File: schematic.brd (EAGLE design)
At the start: 60.9 x 63.2 mm, 40 parts, among them CN1 1X4-BIG, CN2 1X4-BIG, IC3 78TO220, IC4 78TO220

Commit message: Initial board layout
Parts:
- moved R19 36.3 mm to (4.83, 21.8), turned to 180 degrees
- moved R3 25.2 mm to (9.14, 18.8), flipped to the bottom, turned to 180 degrees
- moved R8 24.2 mm to (9.14, 16.8), flipped to the bottom, turned to 180 degrees
- moved R6 22.3 mm to (9.14, 20.8), flipped to the bottom, turned to 180 degrees
- moved R18 18.8 mm to (25.1, 36.3), turned to 90 degrees
- moved R13 17.3 mm to (4.83, 36.3), turned to 270 degrees
- moved R17 17.1 mm to (6.86, 36.3), turned to 90 degrees
- moved R14 15.2 mm to (23.1, 36.3), turned to 270 degrees
- moved R10 13.5 mm to (9.14, 23.6), flipped to the bottom, turned to 180 degrees
- moved R2 13.1 mm to (21.1, 25.7)
- moved R7 13.1 mm to (21.1, 27.7), turned to 180 degrees
- moved R4 12.4 mm to (9.14, 25.7), flipped to the bottom, turned to 180 degrees
- moved R15 12.3 mm to (21.1, 30.7)
- moved R16 12.3 mm to (9.14, 30.7), turned to 180 degrees
- moved R9 12.3 mm to (21.1, 23.6), turned to 0 degrees
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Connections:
- net CTRL_A_3V3: now also U$1.P$23; no longer U$1.P$26
- net CTRL_B_3V3: now also U$1.P$26; no longer U$1.P$23
- net CTRL_G: now also U$1.P$27; no longer U$1.P$28
- net CTRL_R: now also U$1.P$28; no longer U$1.P$27
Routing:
- net +12V: track 0.00 -> 77.9 mm, vias 0 -> 1
- net +5V: track 0.00 -> 46.5 mm
- net N$7: track 0.00 -> 30.4 mm
- net N$5: track 0.00 -> 30.1 mm
- net CTRL_A_3V3: track 0.00 -> 29.2 mm, vias 0 -> 1
- net CTRL_G: track 0.00 -> 25.2 mm
- net CTRL_B: track 0.00 -> 23.3 mm
- net POW_B: track 0.00 -> 18.3 mm
- net N$6: track 0.00 -> 18.2 mm
- net N$8: track 0.00 -> 16.6 mm
- net POW_R: track 0.00 -> 16.4 mm
- net GND: track 0.00 -> 16.3 mm, vias 0 -> 1
- net +3V3: track 0.00 -> 15.8 mm
- net CTRL_B_3V3: track 0.00 -> 11.6 mm, vias 0 -> 1
- net CTRL_B_5V: track 0.00 -> 11.1 mm
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- added copper zone on layer 1, net +3V3
- added copper zone on layer 16, net GND
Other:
- board size 60.9 x 63.2 mm -> 31.9 x 41.1 mm

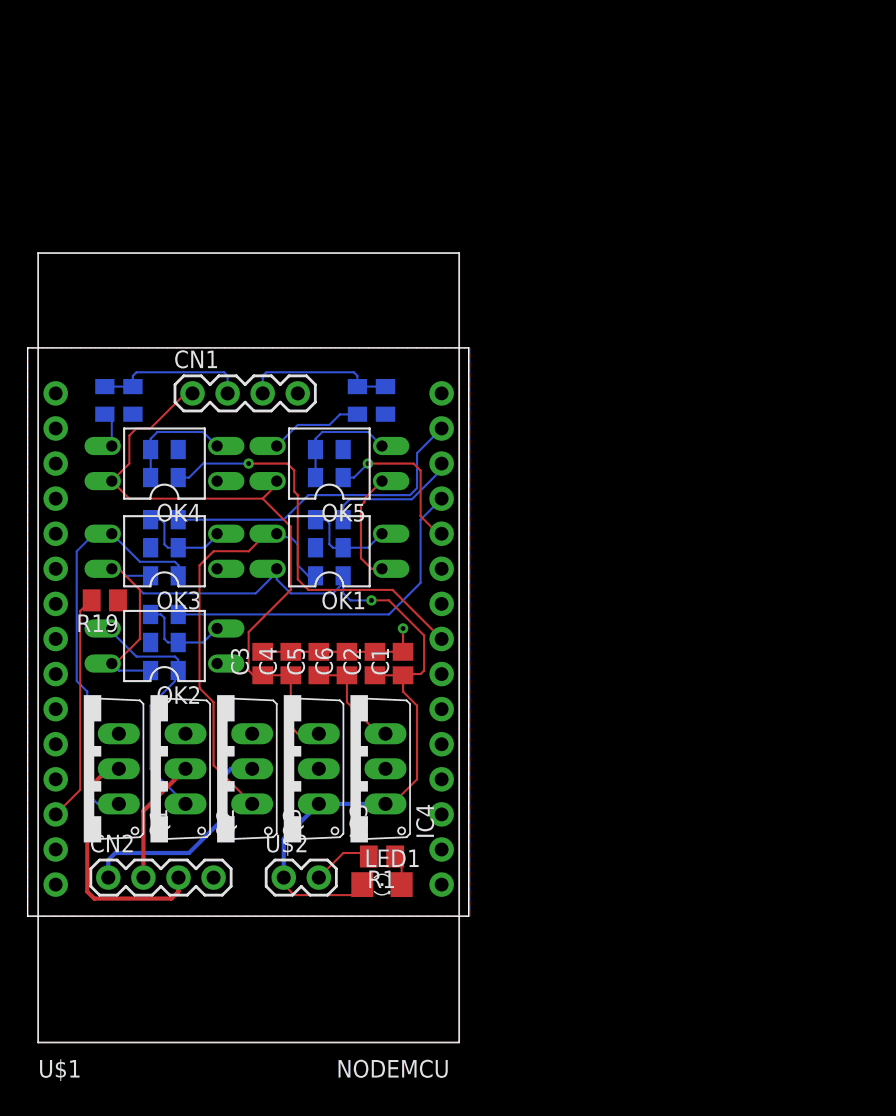
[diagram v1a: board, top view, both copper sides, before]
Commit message: Added board alongation for J4 connector
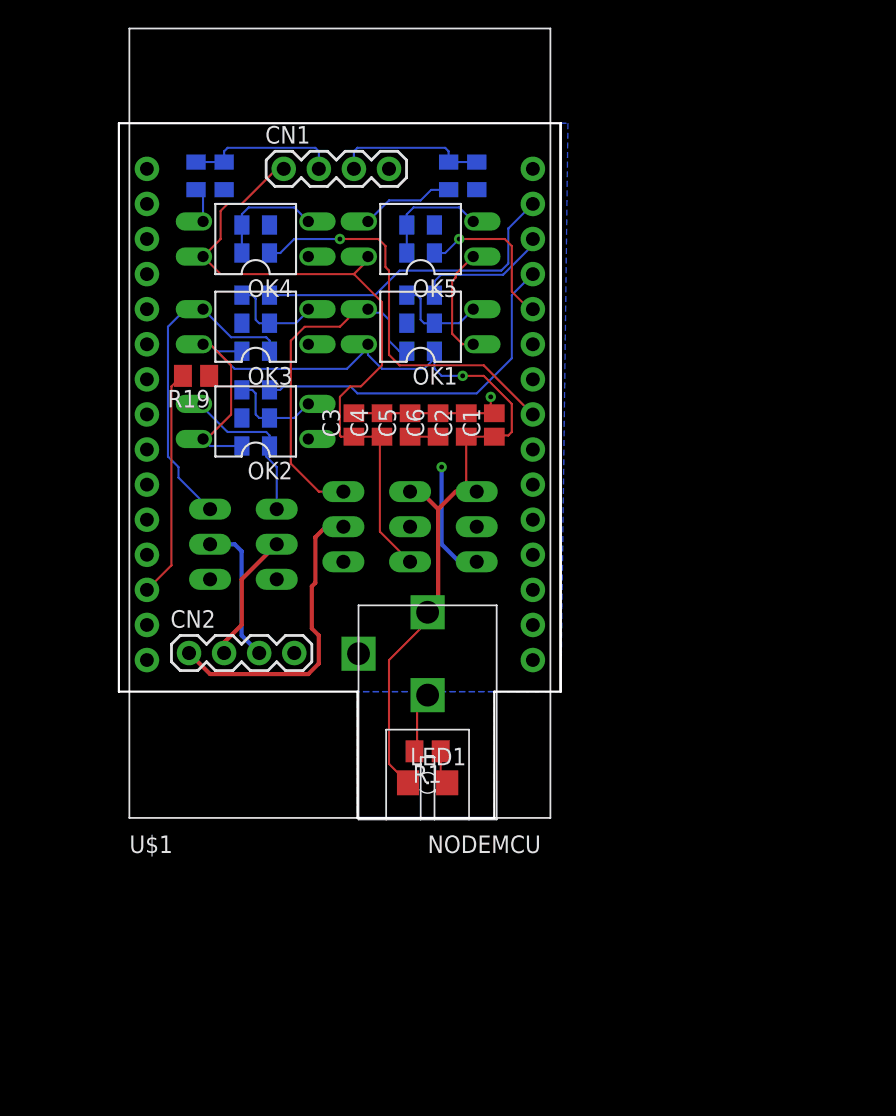
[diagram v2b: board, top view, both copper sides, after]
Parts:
- U$2: value HEADER-2X1 -> J4-2.2X5.1; device z-lib:HEADER-2X1 -> z-lib:J4-2.2X5.1
- moved IC3 18.7 mm to (24.4, 27.2), flipped to the bottom, turned to 270 degrees
- moved IC4 18.7 mm to (29.2, 27.2), flipped to the bottom, turned to 270 degrees
- moved Q3 18.7 mm to (19.6, 27.2), flipped to the bottom, turned to 270 degrees
- moved C1 18.5 mm to (33.0, 34.5)
- moved C2 18.5 mm to (31.0, 34.5)
- moved C3 18.5 mm to (22.9, 34.5)
- moved C4 18.5 mm to (24.9, 34.5)
- moved C5 18.5 mm to (26.9, 34.5)
- moved C6 18.5 mm to (29.0, 34.5)
- moved R6 17.5 mm to (15.7, 37.1)
- moved R8 17.5 mm to (15.7, 33.0)
- moved CN1 17.5 mm to (17.8, 53.1)
- moved OK1 17.5 mm to (27.7, 41.7)
- moved OK2 17.5 mm to (15.7, 34.8)
- moved OK3 17.5 mm to (15.7, 41.7)
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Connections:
- net +12V: now also U$2.P$2; no longer U$2.1
- net GND: now also U$2.P$1, U$2.P$3; no longer U$2.2
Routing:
- net POW_B: track 18.3 -> 10.4 mm
- net N$6: track 18.2 -> 11.7 mm
- net N$5: track 30.1 -> 24.1 mm
- net POW_R: track 16.4 -> 22.2 mm
- net N$7: track 30.4 -> 25.0 mm
- net +5V: track 46.5 -> 50.1 mm
- net +3V3: track 15.8 -> 18.7 mm, vias 0 -> 1
- net +12V: track 77.9 -> 79.7 mm
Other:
- board size 31.9 x 41.1 mm -> 32 x 50.3 mm
